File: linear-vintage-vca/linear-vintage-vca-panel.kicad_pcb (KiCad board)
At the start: 2 copper layers, 70 x 110 mm, 64 parts, among them J1 AudioJack2, J10 Conn_01x10_Socket, J11 Conn_01x04_Pin, J12 Conn_01x04_Socket, J13 AudioJack2, J14 AudioJack2, J15 Conn_02x08_Odd_Even, J2 AudioJack2, J3 AudioJack2, J4 AudioJack2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

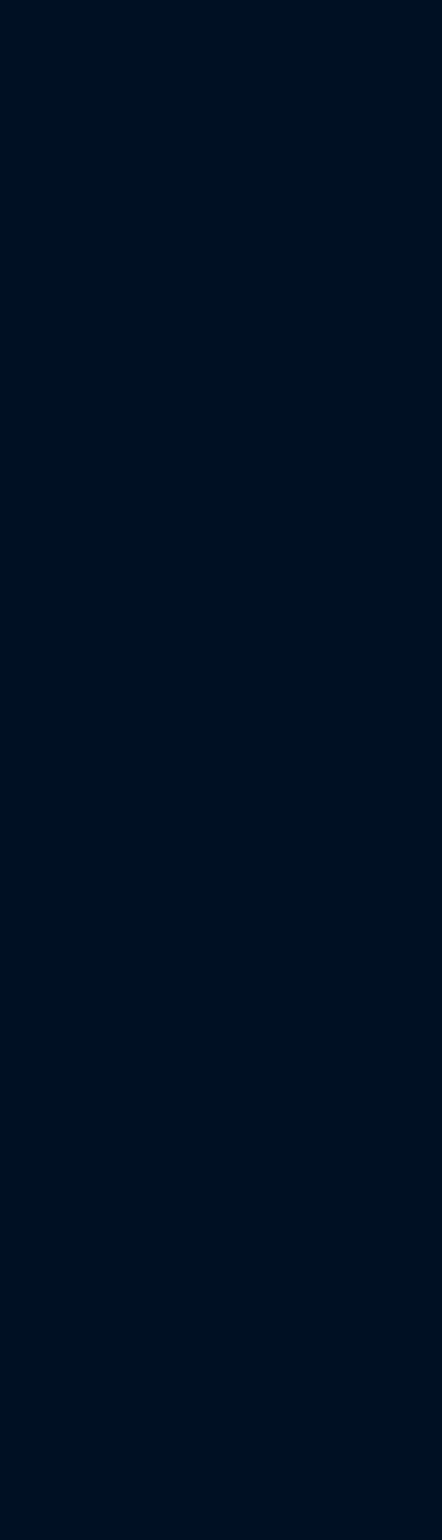
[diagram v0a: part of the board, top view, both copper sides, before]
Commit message: Updated VCA-1 panel
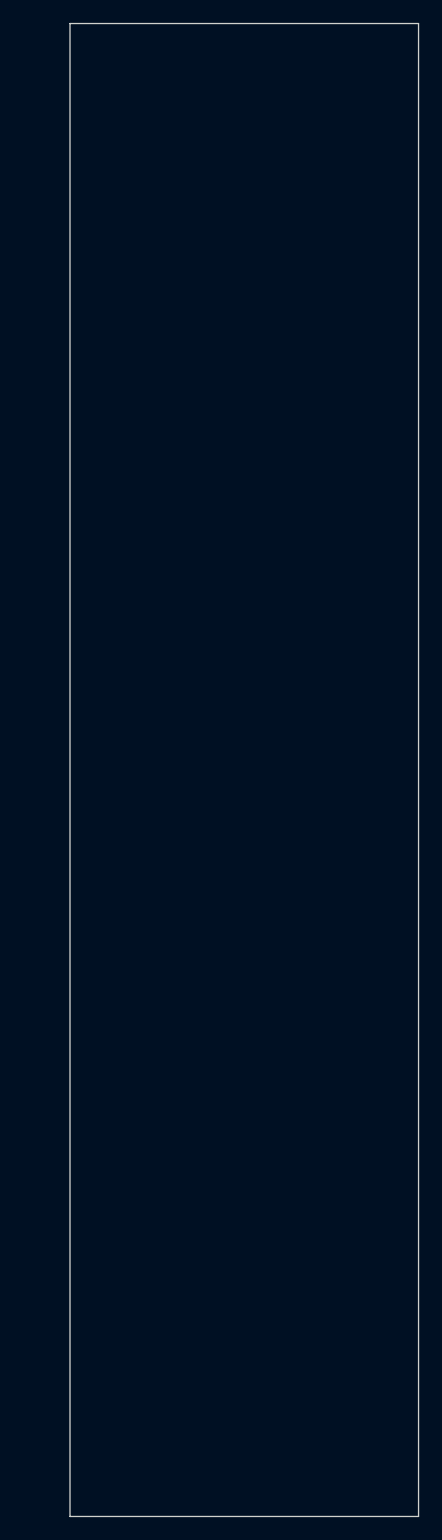
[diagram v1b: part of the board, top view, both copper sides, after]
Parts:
- removed A, B: Board, PCM_kikit:Board
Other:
- board size 70 x 110 mm -> 111.2 x 128.5 mm
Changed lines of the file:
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@@
 		)
 	)
-	(footprint "PCM_kikit:Board"
-		(layer "F.Cu")
-		(at 81.4832 43.688)
-		(descr "Mark board for extraction")
-		(property "Reference" "A"
-			(at -4.5 -5 0)
-			(layer "Dwgs.User")
-			(effects
-				(font
-					(size 1 1)
-					(thickness 0.15)
-				)
-				(justify left)
-			)
-		)
-		(property "Value" "Board"
-			(at -7.25 -5 0)
-			(layer "Dwgs.User")
-			(effects
-				(font
-					(size 1 1)
-					(thickness 0.15)
-				)
-			)
-		)
-		(property "Datasheet" ""
-			(at 0 0 0)
-			(layer "F.Fab")
-			(hide yes)
-			(effects
-				(font
-					(size 1.27 1.27)
-					(thickness 0.15)
-				)
-			)
-		)
-		(property "Description" ""
-			(at 0 0 0)
-			(layer "F.Fab")
-			(hide yes)
-			(effects
-				(font
-					(size 1.27 1.27)
-					(thickness 0.15)
-				)
-			)
-		)
-		(attr board_only exclude_from_pos_files exclude_from_bom allow_missing_courtyard)
-		(fp_line
-			(start -1.25 -4)
-			(end -9.25 -4)
-			(stroke
-				(width 0.2)
-				(type solid)
-			)
-			(layer "Dwgs.User")
-		)
-		(fp_line
-			(start 0 0)
-			(end -1.25 -4)
-			(stroke
-				(width 0.2)
-				(type solid)
-			)
-			(layer "Dwgs.User")
-		)
-		(fp_line
-			(start 0 0)
-			(end -1 -0.5)
-			(stroke
-				(width 0.2)
-				(type solid)
-			)
-			(layer "Dwgs.User")
-		)
-		(fp_line
-			(start 0 0)
-			(end 0.5 -1)
-			(stroke
-				(width 0.2)
-				(type solid)
-			)
-			(layer "Dwgs.User")
-		)
-		(embedded_fonts no)
-	)
 	(footprint "Capacitor_THT:C_Rect_L7.0mm_W2.0mm_P5.00mm"
 		(layer "F.Cu")
@@
 		)
 	)
-	(footprint "PCM_kikit:Board"
-		(layer "F.Cu")
-		(at 35.8394 43.688)
-		(descr "Mark board for extraction")
-		(property "Reference" "B"
-			(at -4.5 -5 0)
-			(layer "Dwgs.User")
-			(effects
-				(font
-					(size 1 1)
-					(thickness 0.15)
-				)
-				(justify left)
-			)
-		)
-		(property "Value" "Board"
-			(at -7.25 -5 0)
-			(layer "Dwgs.User")
-			(effects
-				(font
-					(size 1 1)
-					(thickness 0.15)
-				)
-			)
-		)
-		(property "Datasheet" ""
-			(at 0 0 0)
-			(layer "F.Fab")
-			(hide yes)
-			(effects
-				(font
-					(size 1.27 1.27)
-					(thickness 0.15)
-				)
-			)
-		)
-		(property "Description" ""
-			(at 0 0 0)
-			(layer "F.Fab")
-			(hide yes)
-			(effects
-				(font
-					(size 1.27 1.27)
-					(thickness 0.15)
-				)
-			)
-		)
-		(attr board_only exclude_from_pos_files exclude_from_bom allow_missing_courtyard)
-		(fp_line
-			(start -1.25 -4)
-			(end -9.25 -4)
-			(stroke
-				(width 0.2)
-				(type solid)
-			)
-			(layer "Dwgs.User")
-		)
-		(fp_line
-			(start 0 0)
-			(end -1.25 -4)
-			(stroke
-				(width 0.2)
-				(type solid)
-			)
-			(layer "Dwgs.User")
-		)
-		(fp_line
-			(start 0 0)
-			(end -1 -0.5)
-			(stroke
-				(width 0.2)
-				(type solid)
-			)
-			(layer "Dwgs.User")
-		)
-		(fp_line
-			(start 0 0)
-			(end 0.5 -1)
-			(stroke
-				(width 0.2)
-				(type solid)
-			)
-			(layer "Dwgs.User")
-		)
-		(embedded_fonts no)
-	)
 	(footprint "Diode_THT:D_DO-35_SOD27_P7.62mm_Horizontal"
 		(layer "F.Cu")
@@
 		(stroke
 			(width 0.05)
+			(type solid)
+		)
+		(fill no)
+		(layer "Edge.Cuts")
+	)
+	(gr_rect
+		(start 116.967 34.429)
+		(end 146.967 162.929)
+		(stroke
+			(width 0.05)
